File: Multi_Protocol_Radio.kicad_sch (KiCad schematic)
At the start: 5 parts, among them J10001 Conn_01x06_Pin, J10002 TC2050, U10001 MGM240PB32VNA3

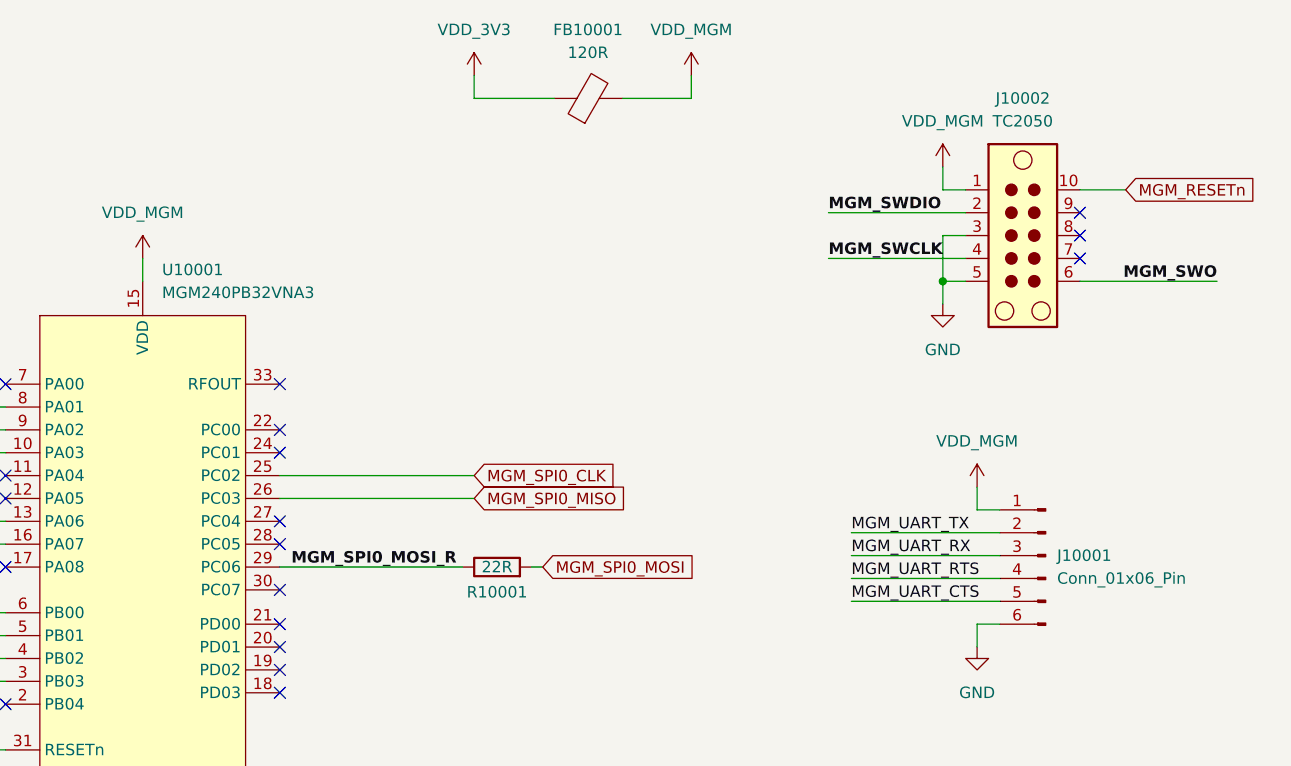
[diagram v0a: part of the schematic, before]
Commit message: Added new radio schematic
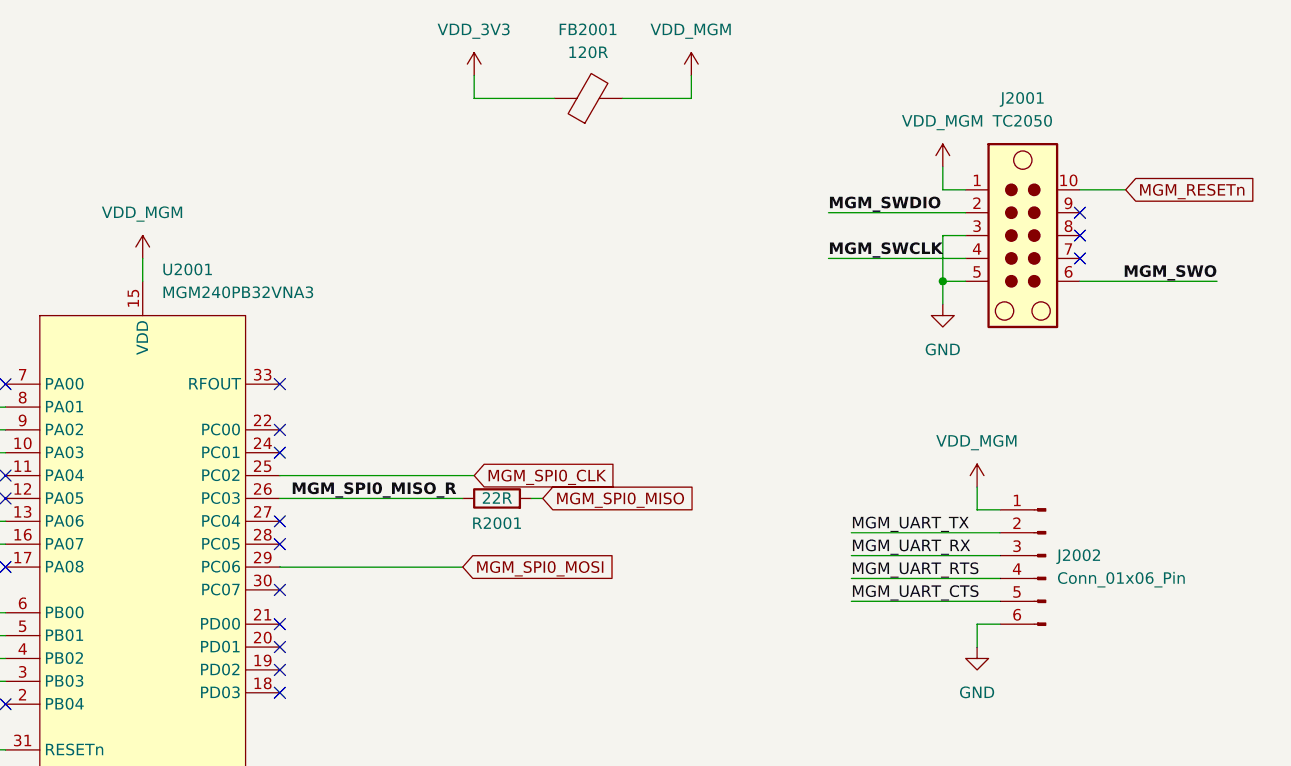
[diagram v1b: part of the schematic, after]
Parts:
- J2002: renamed from J10001; footprint (none) -> Connector_PinHeader_2.54mm:PinHeader_1x06_P2.54mm_Vertical
- renumbered FB10001 to FB2001, J10002 to J2001, R10001 to R2001, U10001 to U2001
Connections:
- net MGM_SPI0_MISO: now also R2001.2; no longer U2001.26 (PC03)
- net MGM_SPI0_MOSI: now also U2001.29 (PC06); no longer R2001.2
- net MGM_SPI0_MOSI_R renamed MGM_SPI0_MISO_R
- net MGM_SPI0_MISO_R: now also U2001.26 (PC03); no longer U2001.29 (PC06)
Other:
- moved on the sheet: R2001
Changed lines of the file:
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@@
 	(wire
 		(pts
-			(xy 120.65 95.25) (xy 142.24 95.25)
+			(xy 120.65 95.25) (xy 140.97 95.25)
 		)
 		(stroke
@@
 	(wire
 		(pts
+			(xy 148.59 95.25) (xy 149.86 95.25)
+		)
+		(stroke
+			(width 0)
+			(type default)
+		)
+	)
+	(wire
+		(pts
 			(xy 184.15 104.14) (xy 200.66 104.14)
-		)
-		(stroke
-			(width 0)
-			(type default)
-		)
-	)
-	(wire
-		(pts
-			(xy 149.86 102.87) (xy 148.59 102.87)
 		)
 		(stroke
@@
 		)
 	)
-	(label "MGM_SPI0_MOSI_R"
-		(at 121.92 102.87 0)
+	(label "MGM_SPI0_MISO_R"
+		(at 121.92 95.25 0)
 		(effects
 			(font
@@
 	(global_label "MGM_SPI0_MISO"
 		(shape input)
-		(at 142.24 95.25 0)
+		(at 149.86 95.25 0)
 		(fields_autoplaced yes)
 		(effects
@@
 		)
 		(property "Intersheetrefs" "${INTERSHEET_REFS}"
-			(at 160.2232 95.25 0)
+			(at 167.8432 95.25 0)
 			(effects
 				(font
@@
 	(global_label "MGM_SPI0_MOSI"
 		(shape input)
-		(at 149.86 102.87 0)
+		(at 140.97 102.87 0)
 		(fields_autoplaced yes)
 		(effects
@@
 		)
 		(property "Intersheetrefs" "${INTERSHEET_REFS}"
-			(at 167.8432 102.87 0)
+			(at 158.9532 102.87 0)
 			(effects
 				(font
@@
 		(dnp no)
 		(fields_autoplaced yes)
-		(property "Reference" "#PWR010006"
+		(property "Reference" "#PWR02007"
 			(at 198.12 118.11 0)
 			(effects
@@
 			(project ""
 				(path "/b43b7bca-e50d-42ec-8ff0-e0016dfefe0a/a72e3651-6b85-4045-b319-d8959d969ced"
-					(reference "#PWR010006")
+					(reference "#PWR02007")
 					(unit 1)
 				)
@@
 		(dnp no)
 		(fields_autoplaced yes)
-		(property "Reference" "U10001"
+		(property "Reference" "U2001"
 			(at 107.5533 69.85 0)
 			(effects
@@
 			(project ""
 				(path "/b43b7bca-e50d-42ec-8ff0-e0016dfefe0a/a72e3651-6b85-4045-b319-d8959d969ced"
-					(reference "U10001")
+					(reference "U2001")
 					(unit 1)
 				)
@@
 		(dnp no)
 		(fields_autoplaced yes)
-		(property "Reference" "#PWR010005"
+		(property "Reference" "#PWR02006"
 			(at 198.12 97.79 0)
 			(effects
@@
 			(project "Leonhart"
 				(path "/b43b7bca-e50d-42ec-8ff0-e0016dfefe0a/a72e3651-6b85-4045-b319-d8959d969ced"
-					(reference "#PWR010005")
+					(reference "#PWR02006")
 					(unit 1)
 				)
@@
 		(dnp no)
 		(fields_autoplaced yes)
-		(property "Reference" "#PWR010001"
+		(property "Reference" "#PWR02008"
 			(at 97.79 144.78 0)
 			(effects
@@
 			(project ""
 				(path "/b43b7bca-e50d-42ec-8ff0-e0016dfefe0a/a72e3651-6b85-4045-b319-d8959d969ced"
-					(reference "#PWR010001")
+					(reference "#PWR02008")
 					(unit 1)
 				)
@@
 		(dnp no)
 		(fields_autoplaced yes)
-		(property "Reference" "#PWR010003"
+		(property "Reference" "#PWR02002"
 			(at 166.37 52.07 0)
 			(effects
@@
 			(project "Leonhart"
 				(path "/b43b7bca-e50d-42ec-8ff0-e0016dfefe0a/a72e3651-6b85-4045-b319-d8959d969ced"
-					(reference "#PWR010003")
+					(reference "#PWR02002")
 					(unit 1)
 				)
@@
 		(dnp no)
 		(fields_autoplaced yes)
-		(property "Reference" "#PWR010002"
+		(property "Reference" "#PWR02001"
 			(at 142.24 52.07 0)
 			(effects
@@
 			(project ""
 				(path "/b43b7bca-e50d-42ec-8ff0-e0016dfefe0a/a72e3651-6b85-4045-b319-d8959d969ced"
-					(reference "#PWR010002")
+					(reference "#PWR02001")
 					(unit 1)
 				)
@@
 		(dnp no)
 		(fields_autoplaced yes)
-		(property "Reference" "FB10001"
+		(property "Reference" "FB2001"
 			(at 154.8892 43.18 90)
 			(effects
@@
 			(project ""
 				(path "/b43b7bca-e50d-42ec-8ff0-e0016dfefe0a/a72e3651-6b85-4045-b319-d8959d969ced"
-					(reference "FB10001")
+					(reference "FB2001")
 					(unit 1)
 				)
@@
 		(dnp no)
 		(fields_autoplaced yes)
-		(property "Reference" "#PWR010004"
+		(property "Reference" "#PWR02004"
 			(at 105.41 72.39 0)
 			(effects
@@
 			(project "Leonhart"
 				(path "/b43b7bca-e50d-42ec-8ff0-e0016dfefe0a/a72e3651-6b85-4045-b319-d8959d969ced"
-					(reference "#PWR010004")
+					(reference "#PWR02004")
 					(unit 1)
 				)
@@
 		(dnp no)
 		(fields_autoplaced yes)
-		(property "Reference" "J10001"
+		(property "Reference" "J2002"
 			(at 207.01 101.5999 0)
 			(effects
@@
 			)
 		)
-		(property "Footprint" ""
+		(property "Footprint" "Connector_PinHeader_2.54mm:PinHeader_1x06_P2.54mm_Vertical"
 			(at 205.74 101.6 0)
 			(effects
@@
 			(project ""
 				(path "/b43b7bca-e50d-42ec-8ff0-e0016dfefe0a/a72e3651-6b85-4045-b319-d8959d969ced"
-					(reference "J10001")
+					(reference "J2002")
 					(unit 1)
 				)
@@
 	(symbol
 		(lib_id "Device:R")
-		(at 144.78 102.87 90)
+		(at 144.78 95.25 90)
 		(unit 1)
 		(exclude_from_sim no)
@@
 		(on_board yes)
 		(dnp no)
-		(property "Reference" "R10001"
-			(at 144.78 105.664 90)
+		(property "Reference" "R2001"
+			(at 144.78 98.044 90)
 			(effects
 				(font
@@
 		)
 		(property "Value" "22R"
-			(at 144.78 102.87 90)
+			(at 144.78 95.25 90)
 			(effects
 				(font
@@
 		)
 		(property "Footprint" ""
-			(at 144.78 104.648 90)
+			(at 144.78 97.028 90)
 			(effects
 				(font
@@
 		)
 		(property "Datasheet" "~"
-			(at 144.78 102.87 0)
+			(at 144.78 95.25 0)
 			(effects
 				(font
@@
 		)
 		(property "Description" "Resistor"
-			(at 144.78 102.87 0)
+			(at 144.78 95.25 0)
 			(effects
 				(font
@@
 			(project ""
 				(path "/b43b7bca-e50d-42ec-8ff0-e0016dfefe0a/a72e3651-6b85-4045-b319-d8959d969ced"
-					(reference "R10001")
+					(reference "R2001")
 					(unit 1)
 				)
@@
 		(dnp no)
 		(fields_autoplaced yes)
-		(property "Reference" "#PWR010007"
+		(property "Reference" "#PWR02005"
 			(at 194.31 80.01 0)
 			(effects
@@
 			(project ""
 				(path "/b43b7bca-e50d-42ec-8ff0-e0016dfefe0a/a72e3651-6b85-4045-b319-d8959d969ced"
-					(reference "#PWR010007")
+					(reference "#PWR02005")
 					(unit 1)
 				)
@@
 		(dnp no)
 		(fields_autoplaced yes)
-		(property "Reference" "J10002"
+		(property "Reference" "J2001"
 			(at 203.2 50.8 0)
 			(effects
@@
 			(project ""
 				(path "/b43b7bca-e50d-42ec-8ff0-e0016dfefe0a/a72e3651-6b85-4045-b319-d8959d969ced"
-					(reference "J10002")
+					(reference "J2001")
 					(unit 1)
 				)
@@
 		(dnp no)
 		(fields_autoplaced yes)
-		(property "Reference" "#PWR010009"
+		(property "Reference" "#PWR02003"
 			(at 194.31 62.23 0)
 			(effects
@@
 			(project "Leonhart"
 				(path "/b43b7bca-e50d-42ec-8ff0-e0016dfefe0a/a72e3651-6b85-4045-b319-d8959d969ced"
-					(reference "#PWR010009")
+					(reference "#PWR02003")
 					(unit 1)
 				)

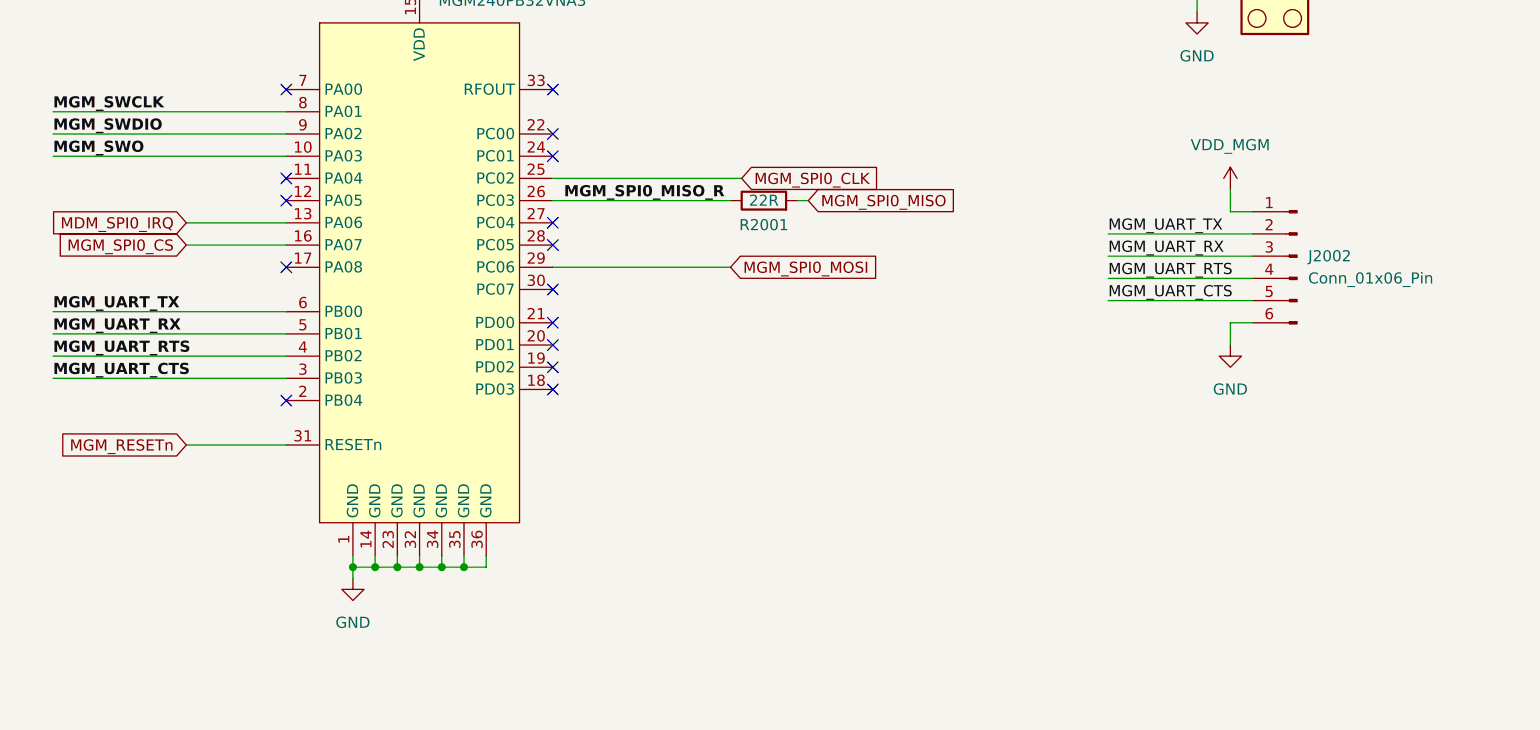
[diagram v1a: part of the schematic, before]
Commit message: Added UART and SPI header pins for MGM240P module options
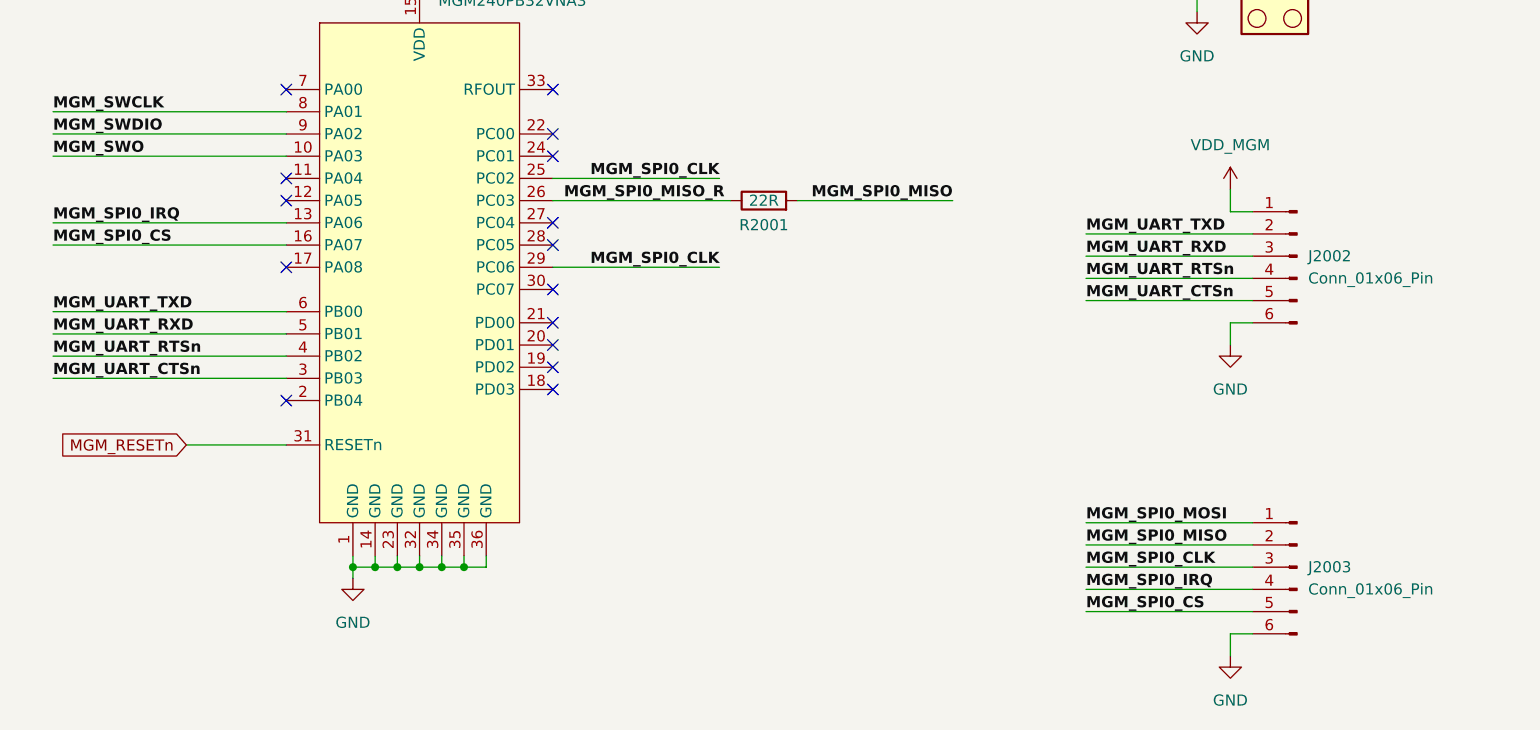
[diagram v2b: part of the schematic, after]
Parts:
- added J2003: Conn_01x06_Pin, Connector_PinHeader_2.54mm:PinHeader_1x06_P2.54mm_Vertical, symbol Connector:Conn_01x06_Pin
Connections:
- net GND: now also J2003.6 (Pin_6)
- net MGM_SPI0_CLK: now also U2001.29 (PC06), J2003.3 (Pin_3)
- net MGM_SPI0_CS: now also J2003.5 (Pin_5)
- net MGM_SPI0_MISO: now also J2003.2 (Pin_2)
- net MGM_SPI0_MOSI: now also J2003.1 (Pin_1); no longer U2001.29 (PC06)
- net MDM_SPI0_IRQ renamed MGM_SPI0_IRQ
- net MGM_SPI0_IRQ: now also J2003.4 (Pin_4)
- net MGM_UART_CTS renamed MGM_UART_CTSn
- net MGM_UART_RTS renamed MGM_UART_RTSn
- net MGM_UART_RX renamed MGM_UART_RXD
- net MGM_UART_TX renamed MGM_UART_TXD

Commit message: Moved around subsections and rerouted RGMII, USBA and USBC
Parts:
- R2001: footprint (none) -> Resistor_SMD:R_0402_1005Metric
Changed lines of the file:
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@@
 			)
 		)
-		(property "Footprint" ""
+		(property "Footprint" "Resistor_SMD:R_0402_1005Metric"
 			(at 144.78 97.028 90)
 			(effects

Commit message: Laid out and routed boot mode resistors
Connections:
- net MGM_SPI0_CLK: no longer U2001.29 (PC06)
- net MGM_SPI0_CS: now also J2003.4 (Pin_4); no longer J2003.5 (Pin_5)
- net MGM_SPI0_IRQ: now also J2003.5 (Pin_5); no longer J2003.4 (Pin_4)
- net MGM_SPI0_MOSI: now also U2001.29 (PC06)

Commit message: Routed SD load switch and system control traces
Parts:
- FB2001: footprint (none) -> Resistor_SMD:R_0402_1005Metric
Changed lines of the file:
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@@
 			)
 		)
-		(property "Footprint" ""
+		(property "Footprint" "Resistor_SMD:R_0402_1005Metric"
 			(at 154.94 52.578 90)
 			(effects
